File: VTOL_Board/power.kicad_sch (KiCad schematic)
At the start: 8 parts, among them J302 19V Input, U301 NCV1117ST50T3G

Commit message: Modify boilerplate for vtol
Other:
- title: Inverted Pendulum Controller -> VTOL Board
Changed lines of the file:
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@@
   (paper "A4")
   (title_block
-    (title "Inverted Pendulum Controller")
+    (title "VTOL Board")
     (date "${ISSUE}")
     (rev "${REVISION}")

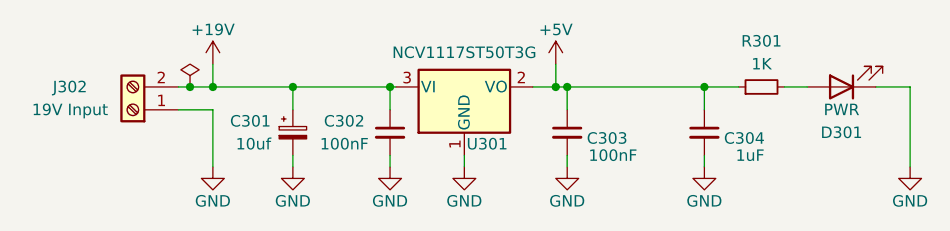
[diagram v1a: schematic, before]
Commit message: Use small hirose connectors
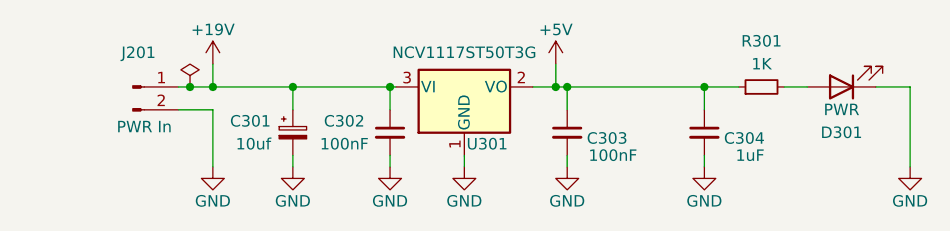
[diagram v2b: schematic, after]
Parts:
- removed J302: 19V Input, TerminalBlock_Phoenix:TerminalBlock_Phoenix_MKDS-3-2-5.08_1x02_P5.08mm_Horizontal, symbol Connector:Screw_Terminal_01x02
- added J201: PWR In, Connector_Hirose:Hirose_DF13-02P-1.25DS_1x02_P1.25mm_Horizontal, symbol Connector:Conn_01x02_Male
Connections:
- net +19V: now also J201.1 (Pin_1)
- net GND: now also J201.2 (Pin_2)
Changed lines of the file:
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@@
     (stroke (width 0) (type default) (color 0 0 0 0))
-  )
-  (symbol (lib_id "Connector:Screw_Terminal_01x02") (at 107.95 90.805 180) (unit 1)
-    (in_bom yes) (on_board yes)
-    (property "Reference" "J302" (id 0) (at 100.965 88.265 0))
-    (property "Value" "19V Input" (id 1) (at 100.965 90.805 0))
-    (property "Footprint" "TerminalBlock_Phoenix:TerminalBlock_Phoenix_MKDS-3-2-5.08_1x02_P5.08mm_Horizontal" (id 2) (at 107.95 90.805 0)
-      (effects (font (size 1.27 1.27)) hide)
-    )
-    (property "Datasheet" "~" (id 3) (at 107.95 90.805 0)
-      (effects (font (size 1.27 1.27)) hide)
-    )
-    (pin "1")
-    (pin "2")
   )
   (symbol (lib_id "power:GND") (at 144.78 97.155 0) (unit 1)
@@
     (pin "3")
   )
+  (symbol (lib_id "Connector:Conn_01x02_Male") (at 107.95 88.265 0) (unit 1)
+    (in_bom yes) (on_board yes)
+    (property "Reference" "J201" (id 0) (at 108.585 84.455 0))
+    (property "Value" "PWR In" (id 1) (at 109.22 92.71 0))
+    (property "Footprint" "Connector_Hirose:Hirose_DF13-02P-1.25DS_1x02_P1.25mm_Horizontal" (id 2) (at 107.95 88.265 0)
+      (effects (font (size 1.27 1.27)) hide)
+    )
+    (property "Datasheet" "~" (id 3) (at 107.95 88.265 0)
+      (effects (font (size 1.27 1.27)) hide)
+    )
+    (pin "1")
+    (pin "2")
+  )
   (symbol (lib_id "Device:C_Small") (at 136.525 93.345 0) (unit 1)
